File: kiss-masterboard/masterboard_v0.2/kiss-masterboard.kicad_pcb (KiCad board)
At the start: 2 copper layers, 187 x 152 mm, 165 parts, among them J1 Cubebatt_host, J10 CRESET, J11 Jumper, J12 Jumper, J13 Conn_02x08_Odd_Even, J14 Conn_02x08_Odd_Even, J15 jmp, J16 jmp, J2 Conn_01x02, J3 Conn_01x02, J4 Conn_01x02, J5 Conn_01x02, J6 Conn_01x02, J7 Conn_01x02, J8 Jumper, J9 jmp, P2 CONN_02X20, U1 TPS54327, U10 CSD86360Q5D, U11 TLV75733PDBV, U13 SN74LVC8T245, U14 W25Q, U17 12MHz, U2 SN74LVC8T245, U4 ICE40UP5k-SG48, U5 SN74LVC8T245, U7 SPH0645LM4H, U8 TLV75709PDBV, U9 TPS53819A

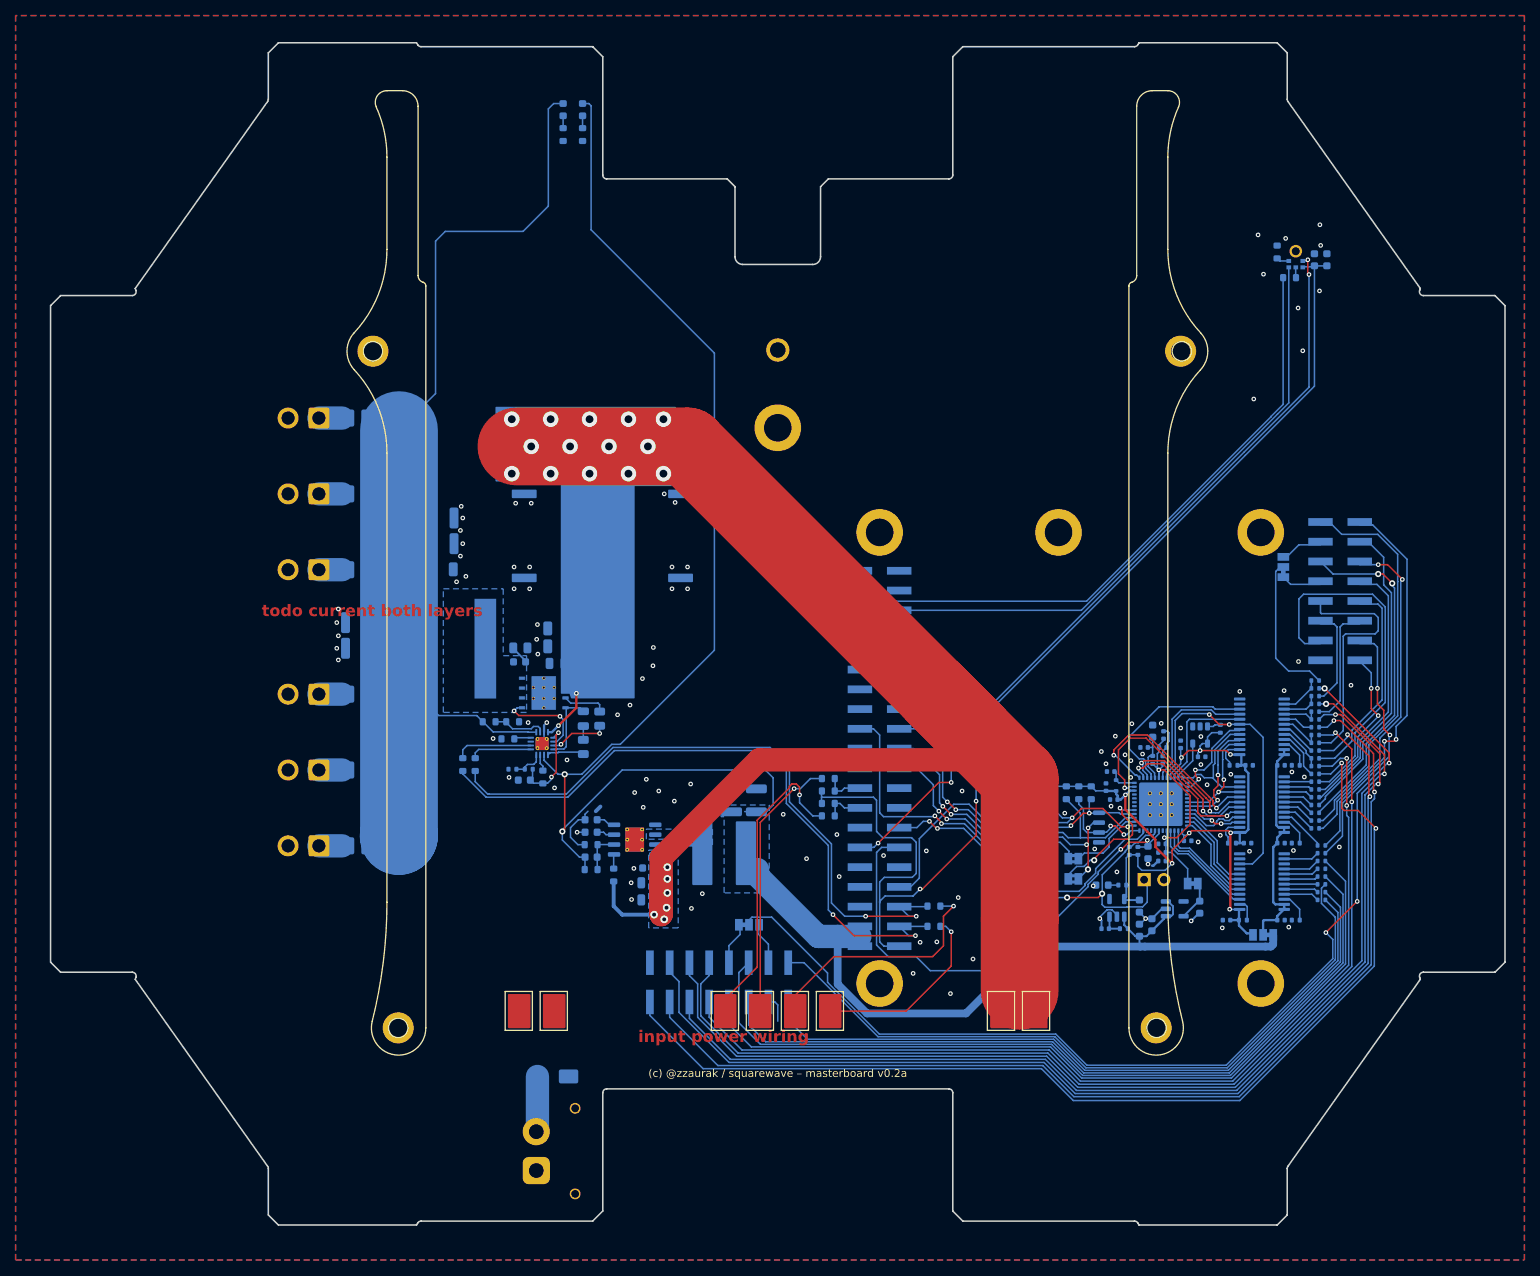
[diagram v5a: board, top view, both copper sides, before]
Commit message: Replaced TPS54327 with TPS56339DDC and adjusted the schematic layout accordingly.
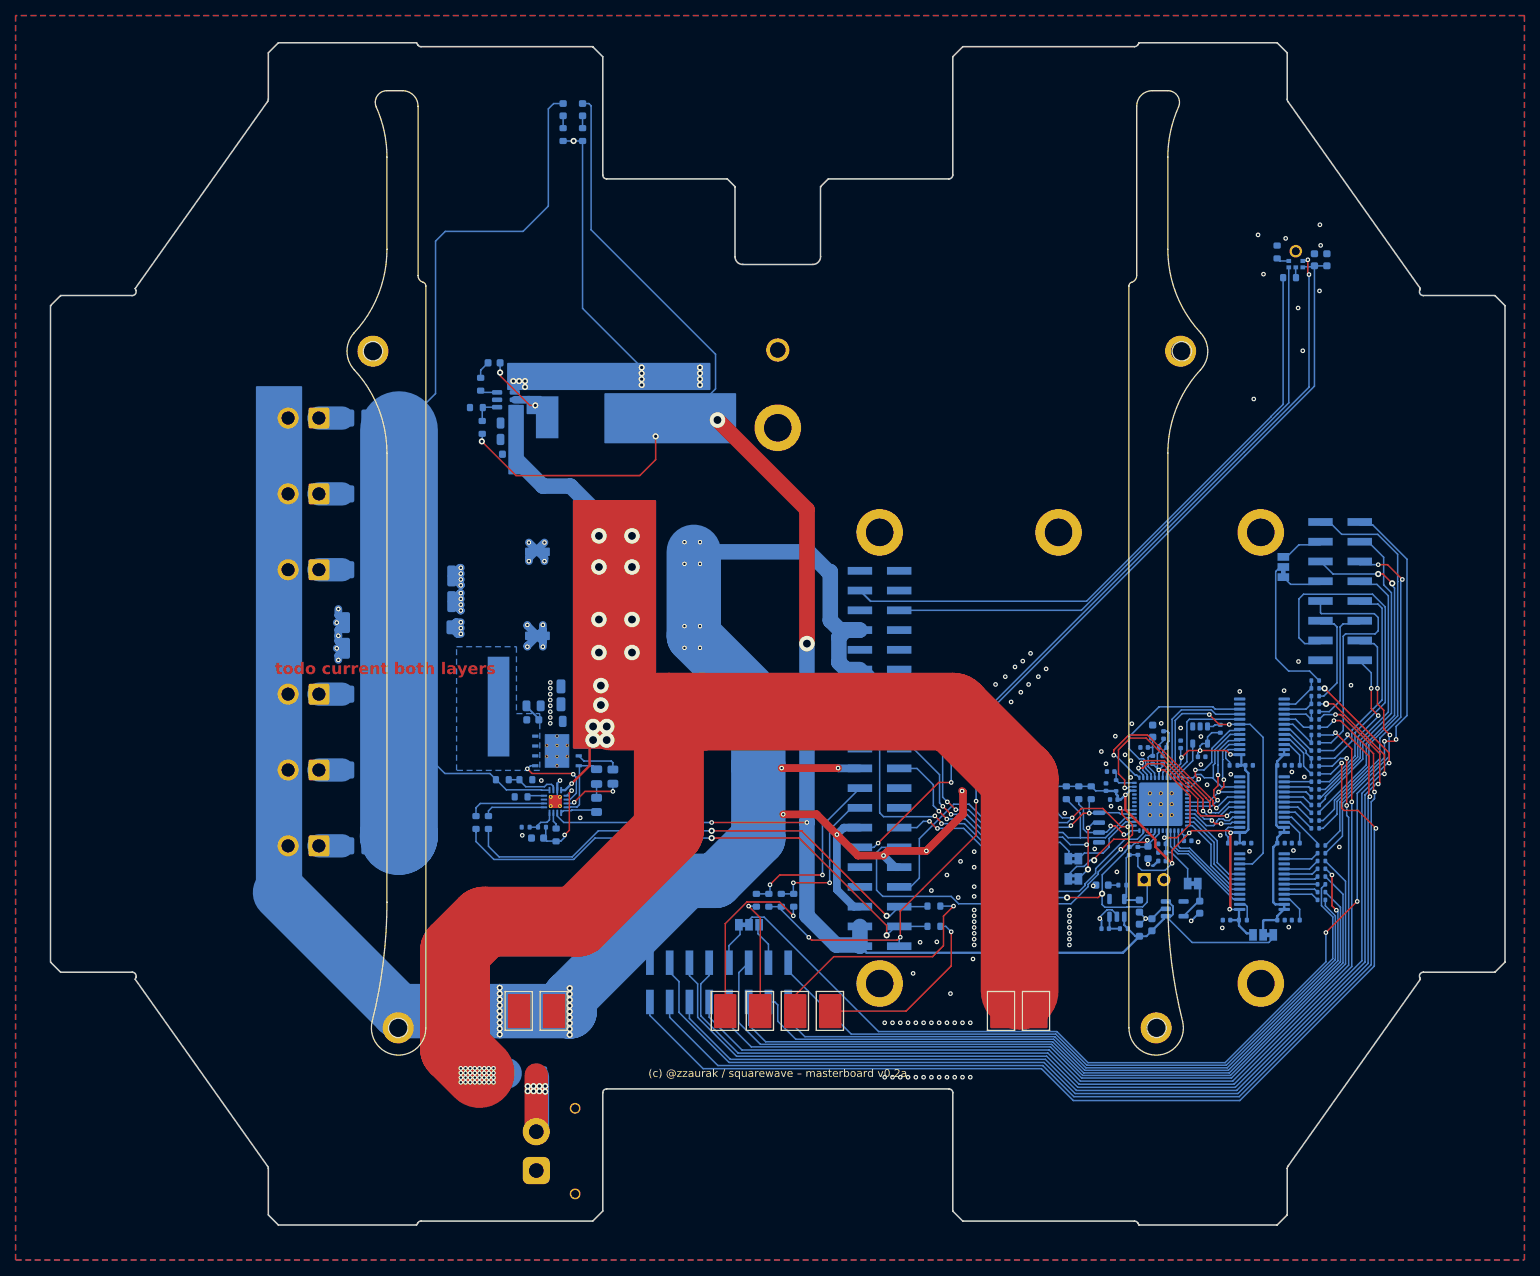
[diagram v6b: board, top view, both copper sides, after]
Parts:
- removed C3: 1µF, Capacitor_SMD:C_0603_1608Metric
- removed C4: 3.3nF, Capacitor_SMD:C_0603_1608Metric
- removed C6: 10pF, Capacitor_SMD:C_0603_1608Metric
- removed U1: TPS54327, Package_SO:HSOP-8-1EP_3.9x4.9mm_P1.27mm_EP2.41x3.1mm_ThermalVias
- added U3: TPS56339DDC, Package_TO_SOT_SMD:SOT-23-6, B.Cu at (73.0, 59.4)
- L8: value 3.3uH, 21m, SRN8040-3R3Y -> 7.6uH 20mOhm; footprint kiss:Bourns_SRN8040 -> Inductor_SMD:L_12x12mm_H4.5mm
- R10: value 137k 1% -> 53.6k %%
- R11: value 23.7k 1% -> 10k %%
- R9: value 10K -> 30
- moved C5 66.3 mm to (71.5, 54.6)
- moved R9 65.4 mm to (69.8, 57.4), turned to 90 degrees
- moved C1 63.9 mm to (73.3, 62.4)
- moved C2 59.8 mm to (73.3, 64.5)
- moved L8 58.8 mm to (83.3, 61.6)
- moved R10 58.5 mm to (70.0, 63.0), turned to -90 degrees
- moved R11 58.1 mm to (69.2, 60.4)
- moved C32 56.2 mm to (73.4, 66.4)
- moved C7 54.5 mm to (92.5, 57.9)
- moved C58 53.3 mm to (96.0, 57.9)
- moved R6 18.2 mm to (105.2, 123.8), turned to -90 degrees
- moved R32 16.0 mm to (106.8, 123.8), turned to -90 degrees
- moved R31 13.8 mm to (108.5, 123.8), turned to -90 degrees
- moved R1 11.7 mm to (110.0, 123.8), turned to -90 degrees
- moved C39 7.64 mm to (81.3, 100.8)
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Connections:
- C5 pad 1: Net-(U1-VBST) -> Net-(C5-Pad1)
- R9 pad 2: /Power+ -> Net-(C5-Pad1)
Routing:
- net GND: track 27.2 -> 316.2 mm, vias 108 -> 188
- net /FPGA Panel Driver/P1_B0x: track 3.46 -> 96.4 mm, vias 0 -> 2
- net Net-(J1-Shutdown): track 34.5 -> 15.2 mm
- net /Raspberry Pi/Powerctrl_off: track 4.94 -> 23.3 mm, vias 0 -> 2
- net /SCL: track 83.6 -> 65.5 mm
- net /SDA: track 85.7 -> 68.4 mm
- net /Raspberry Pi/3v3: track 148.4 -> 131.6 mm, vias 2 -> 3
- net Net-(J1-Buttonpress): track 37.9 -> 23.1 mm
- net /Raspberry Pi/Shutdown_BTN: track 5.02 -> 19.6 mm, vias 0 -> 2
- net /FPGA Panel Driver/iCE_CDONE: track 63.0 -> 51.7 mm
- net Net-(U3-SW): track 2.87 -> 13.2 mm, vias 0 -> 2
- net /Panel_power: track 124.2 -> 133.9 mm
- net Net-(D3-A): track 7.16 -> 14.5 mm, vias 0 -> 8
- net /Power+: track 192.7 -> 198.7 mm, vias 22 -> 47
- net Net-(C5-Pad1): track 0.00 -> 2.32 mm
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- removed copper zone on B.Cu, net /5V_switched
- removed copper zone on B.Cu, net /Power+
- removed copper zone on B.Cu, net Net-(U3-SW)
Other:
- board text removed: "input power wiring"
